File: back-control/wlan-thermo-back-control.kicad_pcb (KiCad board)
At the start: 2 copper layers, 36.2 x 43.8 mm, 13 parts, among them J1 AC / L, J2 AC / N, J3 Signal, J4 Front PWR, Q1 SS8050-G, U2 WX-DC12003, U3 PC817

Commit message: First version fitting together
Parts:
- J1: footprint TerminalBlock:TerminalBlock_bornier-3_P5.08mm -> Chof747 Footprints:TerminalBlock_2_P10.16mm
- moved G*** 116.1 mm to (78.8, 80.9), turned to -90 degrees
- moved J1 10.3 mm to (101.2, 109.3), turned to 90 degrees
- moved J3 0.64 mm to (83.4, 100.0)
- moved J4 0.64 mm to (83.4, 72.8)
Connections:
- J1 pad 2: unconnected-(J1-Pin_2-Pad2) -> L
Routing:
- net LOAD_OUT: track 15.6 -> 0.00 mm, vias 4 -> 7
- net N: track 5.08 -> 19.9 mm
- net L: track 42.1 -> 29.8 mm, vias 4 -> 7
- net /RELAY_GND: track 30.1 -> 27.0 mm
- net +5V: track 48.1 -> 47.5 mm
- added copper zone on B.Cu, net L
- added copper zone on B.Cu, net LOAD_OUT
- added copper zone on F.Cu, net N
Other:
- outline, holes or cut-outs redrawn
- board text added: "W-Lan Thermo Back Control v1.0 (2023)"

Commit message: Corrected traces and spacings for assembly
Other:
- outline, holes or cut-outs redrawn
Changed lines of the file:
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@@
     (property "ki_keywords" "connector")
     (attr through_hole)
-    (fp_text reference "J1" (at -3.683 -2.8194) (layer "F.SilkS")
+    (fp_text reference "J1" (at 13.997 2.8064) (layer "F.SilkS")
         (effects (font (size 1 1) (thickness 0.15)))
     )
@@
   (gr_arc (start 69.596 71.342) (mid 70.181786 69.927786) (end 71.596 69.342)
     (stroke (width 0.1) (type default)) (layer "Edge.Cuts"))
-  (gr_line (start 90.47 106.6) (end 90.47 102.05)
+  (gr_line (start 88.6 105.825) (end 88.6 102.05)
     (stroke (width 0.1) (type default)) (layer "Edge.Cuts"))
-  (gr_line (start 90.47 102.05) (end 105.76 102.04)
+  (gr_line (start 88.6 102.05) (end 105.76 102.05)
     (stroke (width 0.1) (type default)) (layer "Edge.Cuts"))
   (gr_arc (start 71.596 113.157) (mid 70.181786 112.571214) (end 69.596 111.157)
@@
   (gr_line (start 103.759 113.157) (end 71.596 113.157)
     (stroke (width 0.1) (type default)) (layer "Edge.Cuts"))
-  (gr_line (start 105.759 111.157) (end 105.76 106.61)
+  (gr_line (start 105.759 111.157) (end 105.76 105.835)
     (stroke (width 0.1) (type default)) (layer "Edge.Cuts"))
-  (gr_line (start 105.76 106.61) (end 90.47 106.6)
+  (gr_line (start 105.76 105.835) (end 88.6 105.825)
     (stroke (width 0.1) (type default)) (layer "Edge.Cuts"))
   (gr_line locked (start 105.759 71.342) (end 105.759 100)
@@
   (gr_line (start 69.596 111.157) (end 69.596 71.342)
     (stroke (width 0.1) (type default)) (layer "Edge.Cuts"))
-  (gr_line (start 105.759 100) (end 105.76 102.04)
+  (gr_line (start 105.759 100) (end 105.76 102.05)
     (stroke (width 0.1) (type default)) (layer "Edge.Cuts"))
   (gr_arc (start 105.759 111.157) (mid 105.173214 112.571214) (end 103.759 113.157)
@@
       (pts
         (xy 106.426 113.157)
-        (xy 106.426 106.68)
-        (xy 89.535 106.68)
+        (xy 106.466 105.87)
+        (xy 89.575 105.87)
         (xy 89.535 113.157)
       )
@@
     (polygon
       (pts
-        (xy 106.553 101.981)
-        (xy 106.553 93.472)
-        (xy 89.662 93.472)
-        (xy 89.662 101.981)
+        (xy 106.553 102.009)
+        (xy 106.553 94.516)
+        (xy 89.662 94.516)
+        (xy 89.662 102.009)
       )
     )

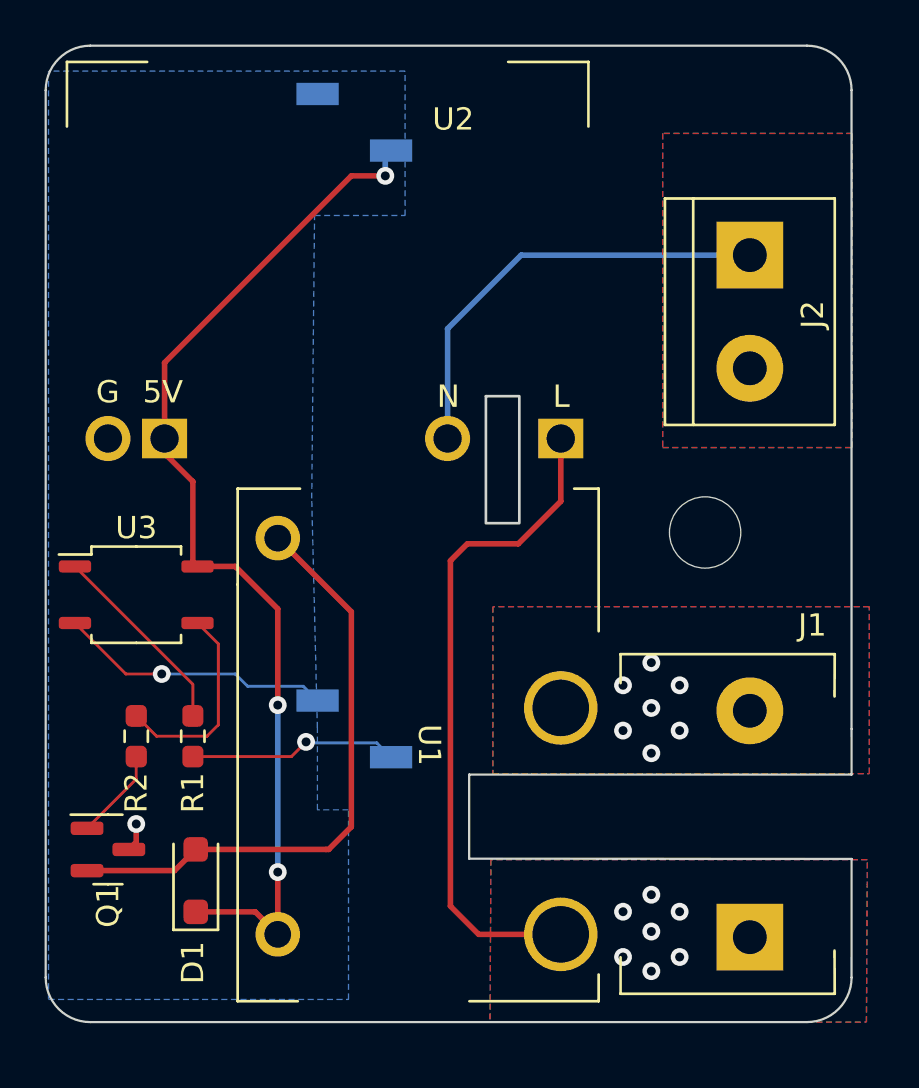
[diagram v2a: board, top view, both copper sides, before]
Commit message: Corrected wrongly placed footprint for relay
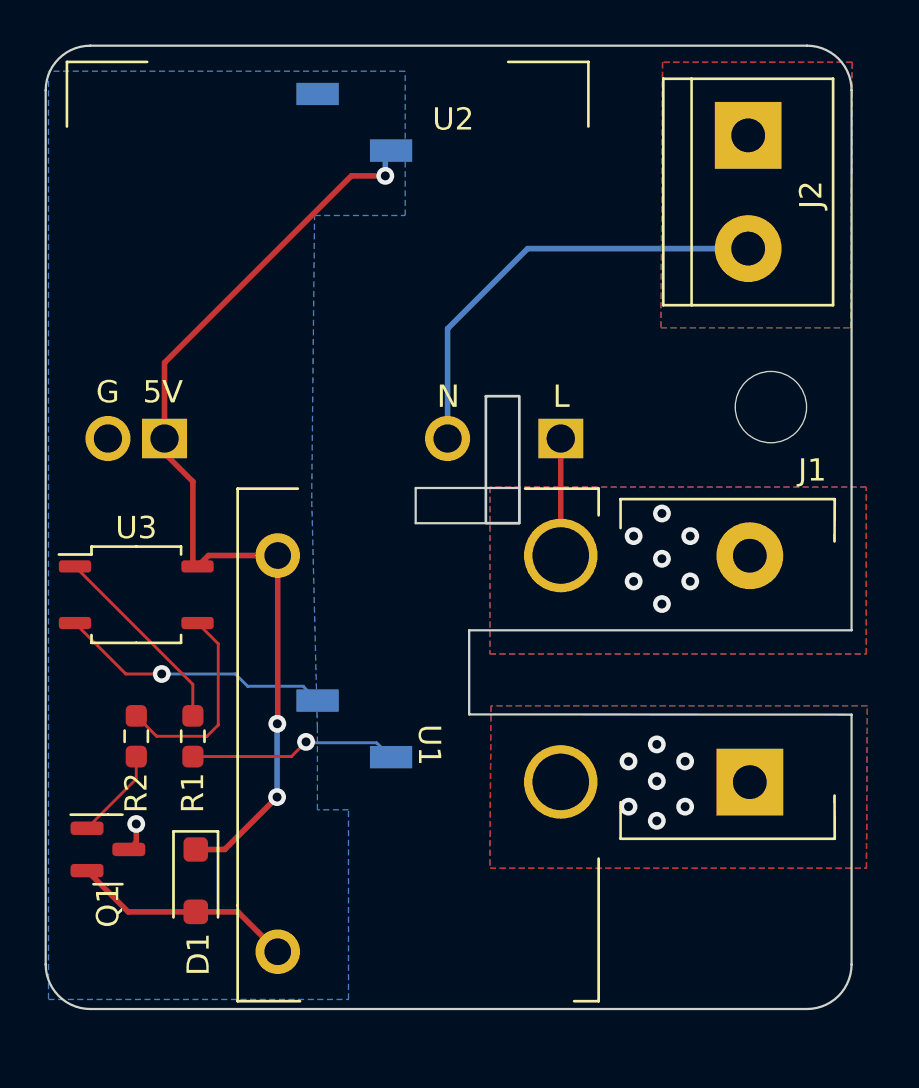
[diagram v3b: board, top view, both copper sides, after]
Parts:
- moved J1 6.96 mm to (101.2, 102.4)
- moved H1 6.35 mm to (102.1, 85.6)
- moved J2 5.37 mm to (101.1, 73.4)
- turned D1 to -90 degrees
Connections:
- J1 pad 1: LOAD_OUT -> L
- J1 pad 2: L -> LOAD_OUT
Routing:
- net L: track 29.8 -> 5.25 mm
- net /RELAY_GND: track 27.0 -> 10.1 mm
- net +5V: track 47.5 -> 43.7 mm
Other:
- board size 36.2 x 43.8 mm -> 36.2 x 43.2 mm
